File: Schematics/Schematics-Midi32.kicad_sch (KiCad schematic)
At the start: 1 part

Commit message: Prelude to split configurations.
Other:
- sheet Digital-2-Optical renamed Digital-2

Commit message: Current State with updated LFO for original board.
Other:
- sheet LFO-1 renamed LFO-2
- sheet LFO-2: file LFO-1.kicad_sch -> LFO-2.kicad_sch
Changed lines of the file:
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@@
 		)
 	)
-	(hierarchical_label "LFO1"
+	(hierarchical_label "LFO2"
 		(shape output)
 		(at 78.994 82.55 0)
@@
 		)
 	)
-	(hierarchical_label "LFO1"
+	(hierarchical_label "LFO2"
 		(shape input)
 		(at 78.74 73.66 0)
@@
 			(color 0 0 0 0.0000)
 		)
-		(property "Sheetname" "LFO-1"
+		(property "Sheetname" "LFO-2"
 			(at 85.344 81.28 0)
 			(effects
@@
 			)
 		)
-		(property "Sheetfile" "LFO-1.kicad_sch"
+		(property "Sheetfile" "LFO-2.kicad_sch"
 			(at 77.724 97.8666 0)
 			(effects

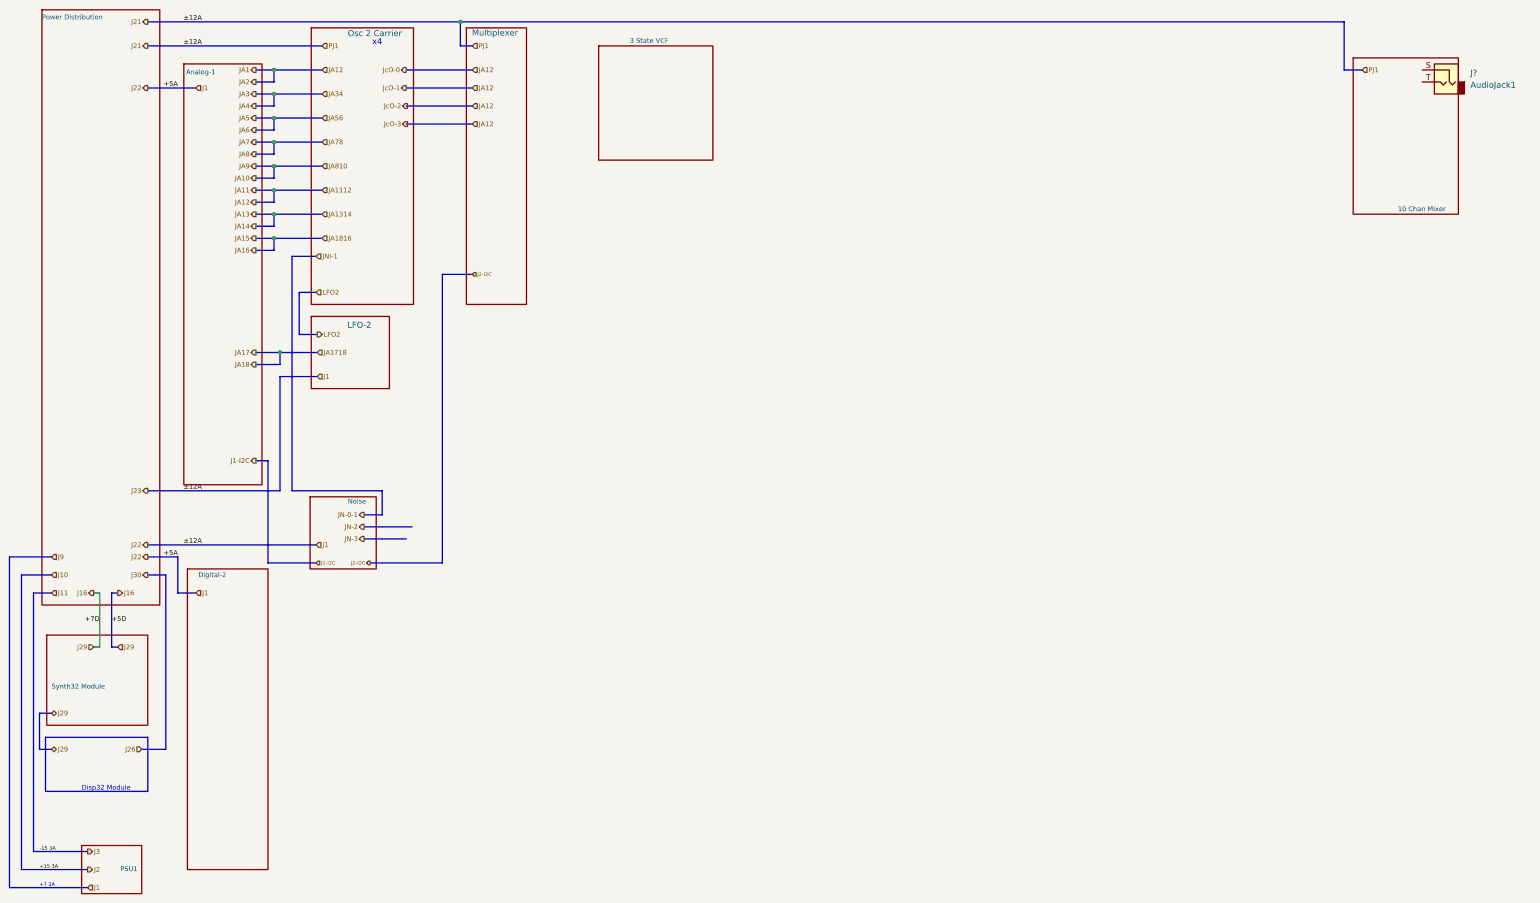
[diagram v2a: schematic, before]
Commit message: Upgreade byte value interface to short.  First stage of refactoring midi input for rotory encoders.  Still needs scaling.
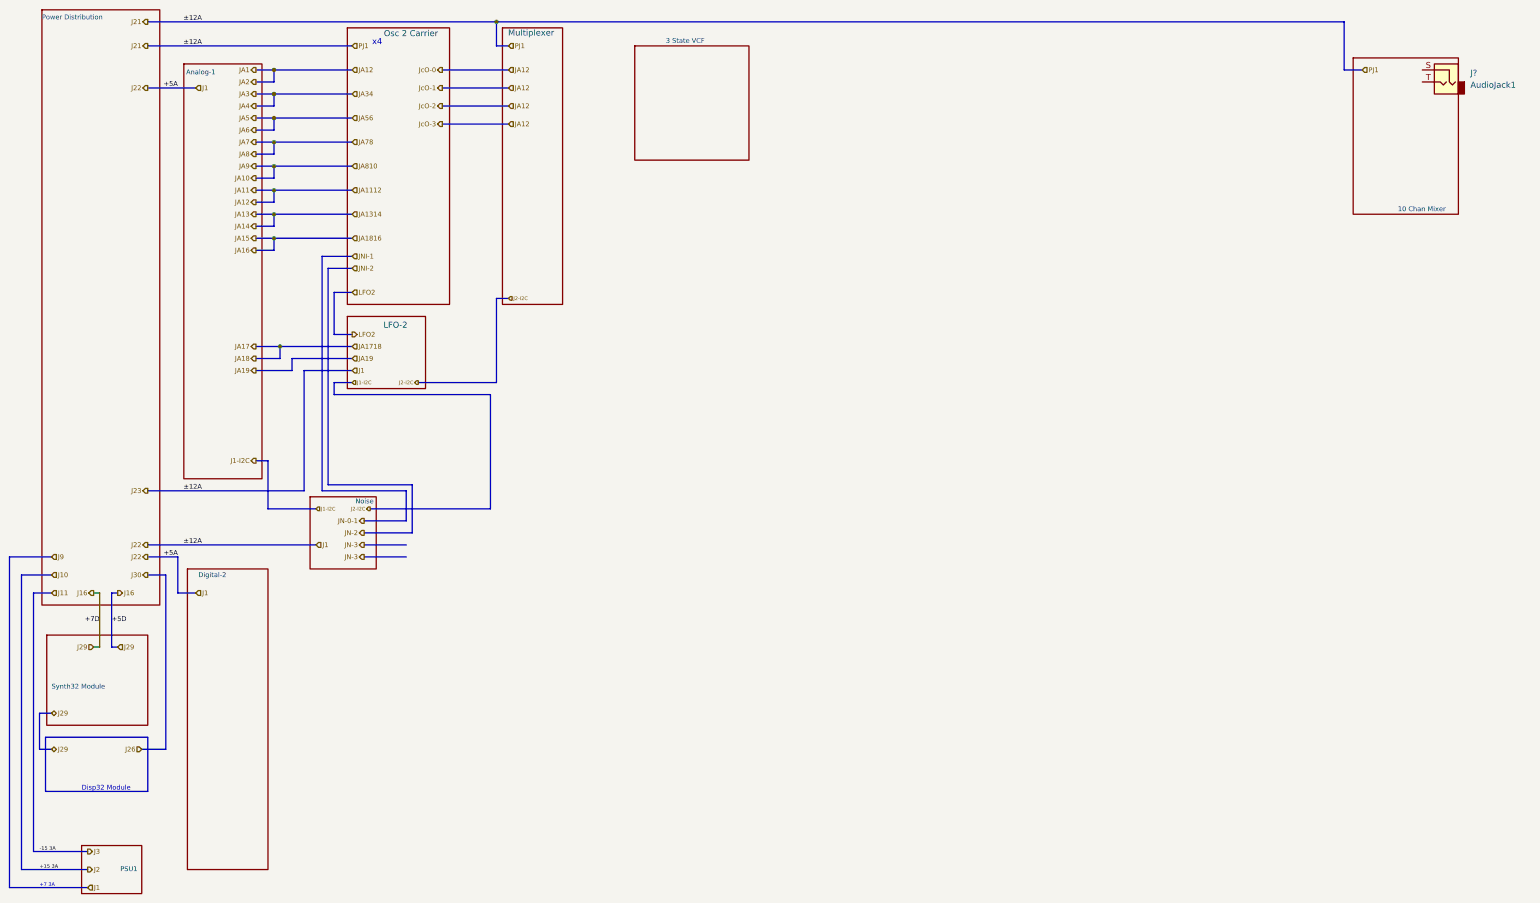
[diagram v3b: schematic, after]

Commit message: Adding in partion LFO-2.  Changed keboard buttons to momentary and encoders to just direction.
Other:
- sheet Digital-2 renamed Digital-1
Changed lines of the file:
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@@
 			(color 0 0 0 0.0000)
 		)
-		(property "Sheetname" "Digital-2"
+		(property "Sheetname" "Digital-1"
 			(at 53.8661 133.9228 0)
 			(effects
